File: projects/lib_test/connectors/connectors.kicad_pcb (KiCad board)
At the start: 2 copper layers, 80 x 60 mm, 0 parts

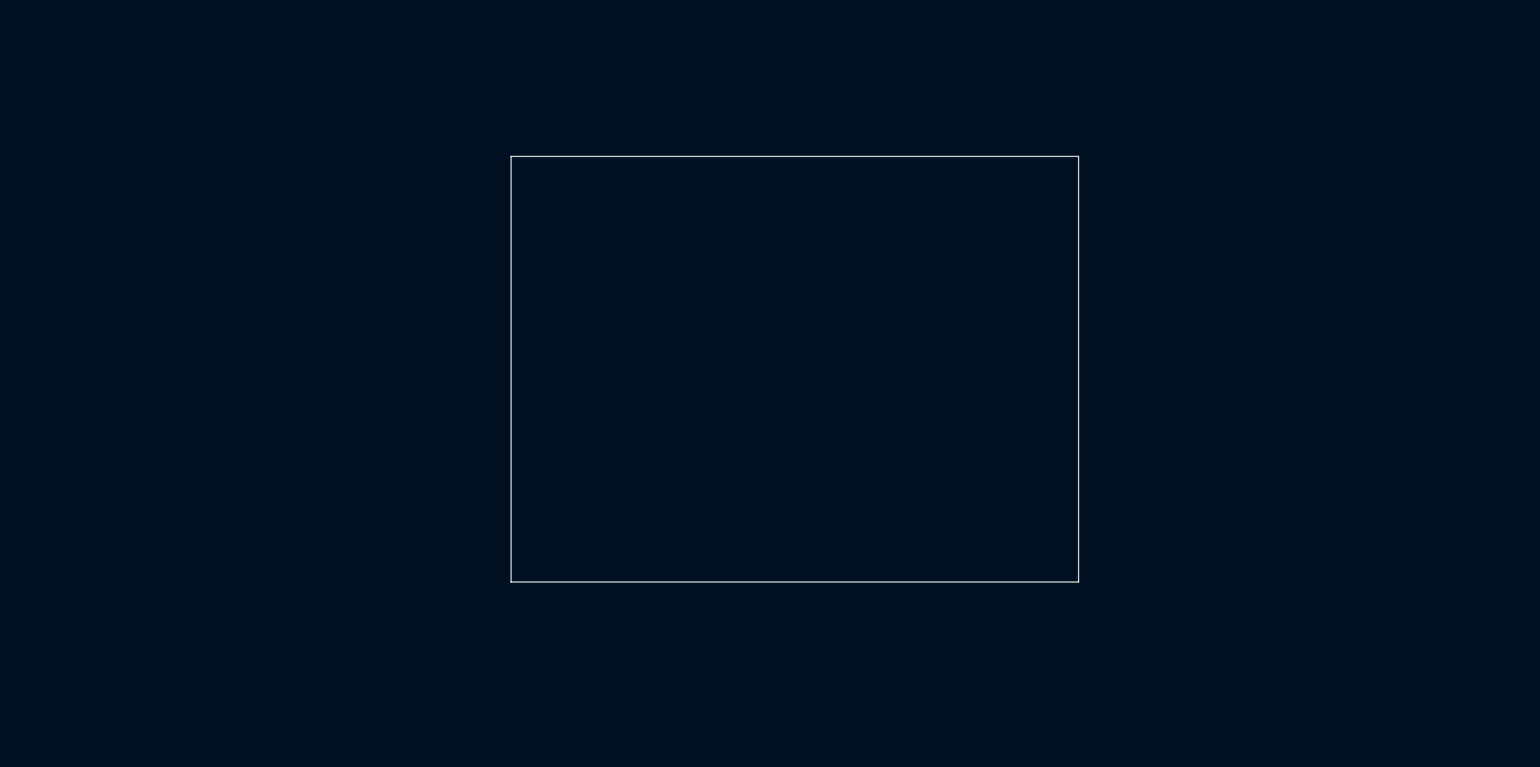
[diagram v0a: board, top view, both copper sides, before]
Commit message: updated test project for connectors
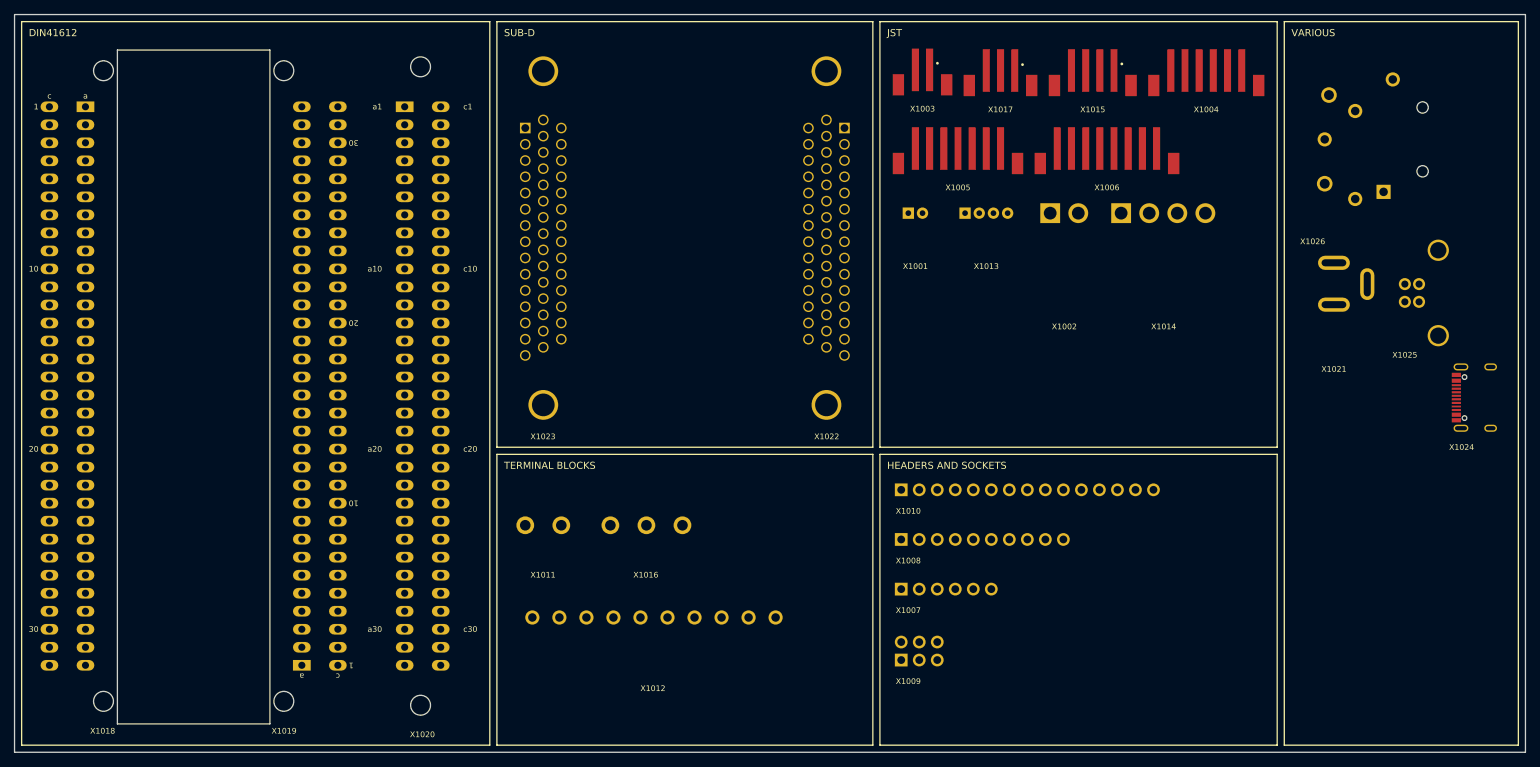
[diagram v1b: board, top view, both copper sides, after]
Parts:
- added X1001: 1x02_PH, lily_footprints:con_jst_1x02_ph_2.00mm_right_angle_th, F.Cu at (166.0, 78.0)
- added X1002: 1x02_VH, lily_footprints:con_jst_1x02_vh_3.96mm_right_angle_th, F.Cu at (186.0, 78.0)
- added X1003: 1x02_PH, lily_footprints:con_jst_1x02_ph_2.00mm_straight_smd, F.Cu at (168.0, 59.9)
- added X1004: 1x06_PH, lily_footprints:con_jst_1x06_ph_2.00mm_straight_smd, F.Cu at (208.0, 60.0)
- added X1005: 1x07_PH, lily_footprints:con_jst_1x07_ph_2.00mm_straight_smd, F.Cu at (173.0, 71.0)
- added X1006: 1x08_PH, lily_footprints:con_jst_1x08_ph_2.00mm_straight_smd, F.Cu at (194.0, 71.0)
- added X1007: 1x06, lily_footprints:con_header_1x06_2.54mm_th, F.Cu at (165.0, 131.0)
- added X1008: 1x10, lily_footprints:con_header_1x10_2.54mm_th, F.Cu at (165.0, 124.0)
- added X1009: 2x03, lily_footprints:con_header_2x03_2.54mm_th, F.Cu at (165.0, 141.0)
- added X1010: 1x15, lily_footprints:con_socket_1x15_2.54mm_straight_th, F.Cu at (165.0, 117.0)
- added X1011: 2p_5.08, lily_footprints:con_terminal_block_2p_5.08mm_th, F.Cu at (112.0, 122.0)
- added X1012: socket_male, lily_footprints:con_terminal_socket_male_10p_3.81mm_right_angle_th, F.Cu at (113.0, 135.0)
- added X1013: 1x04_PH, lily_footprints:con_jst_1x04_ph_2.00mm_right_angle_th, F.Cu at (174.0, 78.0)
- added X1014: 1x04_VH, lily_footprints:con_jst_1x04_vh_3.96mm_right_angle_th, F.Cu at (196.0, 78.0)
- added X1015: 1x04_PH, lily_footprints:con_jst_1x04_ph_2.00mm_straight_smd, F.Cu at (192.0, 60.0)
- added X1016: 3p_5.08, lily_footprints:con_terminal_block_3p_5.08mm_th, F.Cu at (124.0, 122.0)
- added X1017: 1x03_PH, lily_footprints:con_jst_1x03_ph_2.00mm_straight_smd, F.Cu at (179.0, 60.0)
- added X1018: din41612_plug, lily_footprints:con_din41612_plug_64p_a+c_right_angle_th, F.Cu at (50.0, 63.0)
- added X1019: din41612_receptacle, lily_footprints:con_din41612_receptacle_64p_a+c_right_angle_th, F.Cu at (80.5, 141.7)
- added X1020: din41612_receptacle, lily_footprints:con_din41612_receptacle_64p_a+c_straight_th, F.Cu at (95.0, 63.0)
- added X1021: dc_005, lily_footprints:con_dc_jack_dc_005_th, F.Cu at (226.0, 98.6)
- added X1022: sub_d_hd_plug, lily_footprints:con_sub_d_hd_plug_44p_right_angle_th, F.Cu at (157.0, 66.0)
- added X1023: sub_d_hd_receptacle, lily_footprints:con_sub_d_hd_receptacle_44p_right_angle_th, F.Cu at (112.0, 66.0)
- added X1024: usb_c, lily_footprints:con_usb_c_receptacle_16p, F.Cu at (246.0, 104.0)
- added X1025: usb_b, lily_footprints:con_usb_b_receptacle_th, F.Cu at (236.0, 88.0)
- added X1026: RCJ6A-H, lily_footprints:con_xlr_jack_rcj6fa-h_th, F.Cu at (233.0, 75.0)
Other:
- board size 80 x 60 mm -> 213 x 104 mm
- board text added: "DIN41612"
- board text added: "HEADERS AND SOCKETS"
- board text added: "JST"
- board text added: "SUB-D"
- board text added: "TERMINAL BLOCKS"
- board text added: "VARIOUS"

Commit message: updated test projects
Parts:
- added X1015: 1x03_PH, lily_footprints:con_jst_1x03_ph_2.00mm_right_angle_th, F.Cu at (166.0, 90.0)
- added X1027: SMA, lily_footprints:con_rf_sma_right_angle_th, F.Cu at (247.0, 117.0)
- added X1029: TC2030-IDC, lily_footprints:con_tc2030_idc_lock, F.Cu at (226.0, 107.0)
- renumbered X1016 to X1013, X1017 to X1014, X1013 to X1016, X1014 to X1017, X1015 to X1018, X1018 to X1019, X1019 to X1020, X1020 to X1021, X1021 to X1022, X1022 to X1023, X1023 to X1024, X1024 to X1025, X1025 to X1026, X1026 to X1028
